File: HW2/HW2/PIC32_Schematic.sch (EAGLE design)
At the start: 22 parts

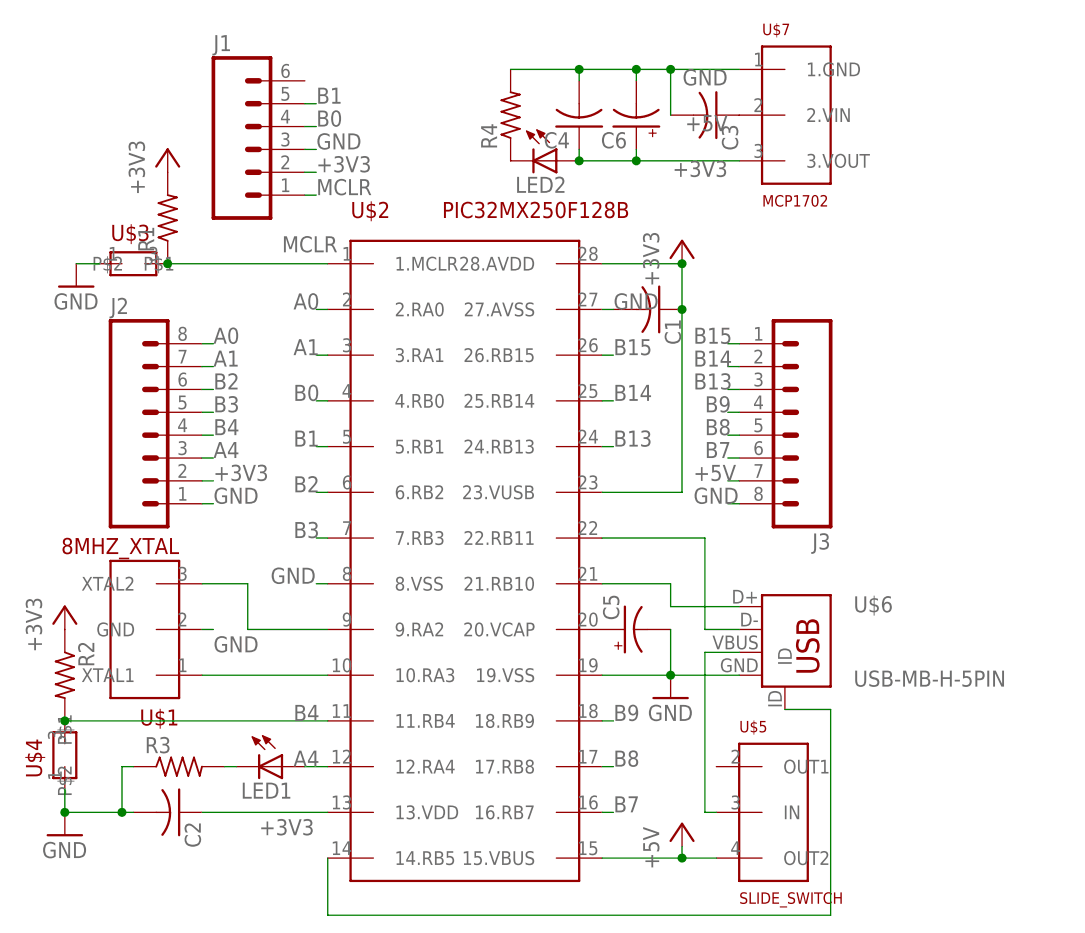
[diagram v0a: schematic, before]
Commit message: Entire schematic is connected (verified).
Formatting and value setting required!
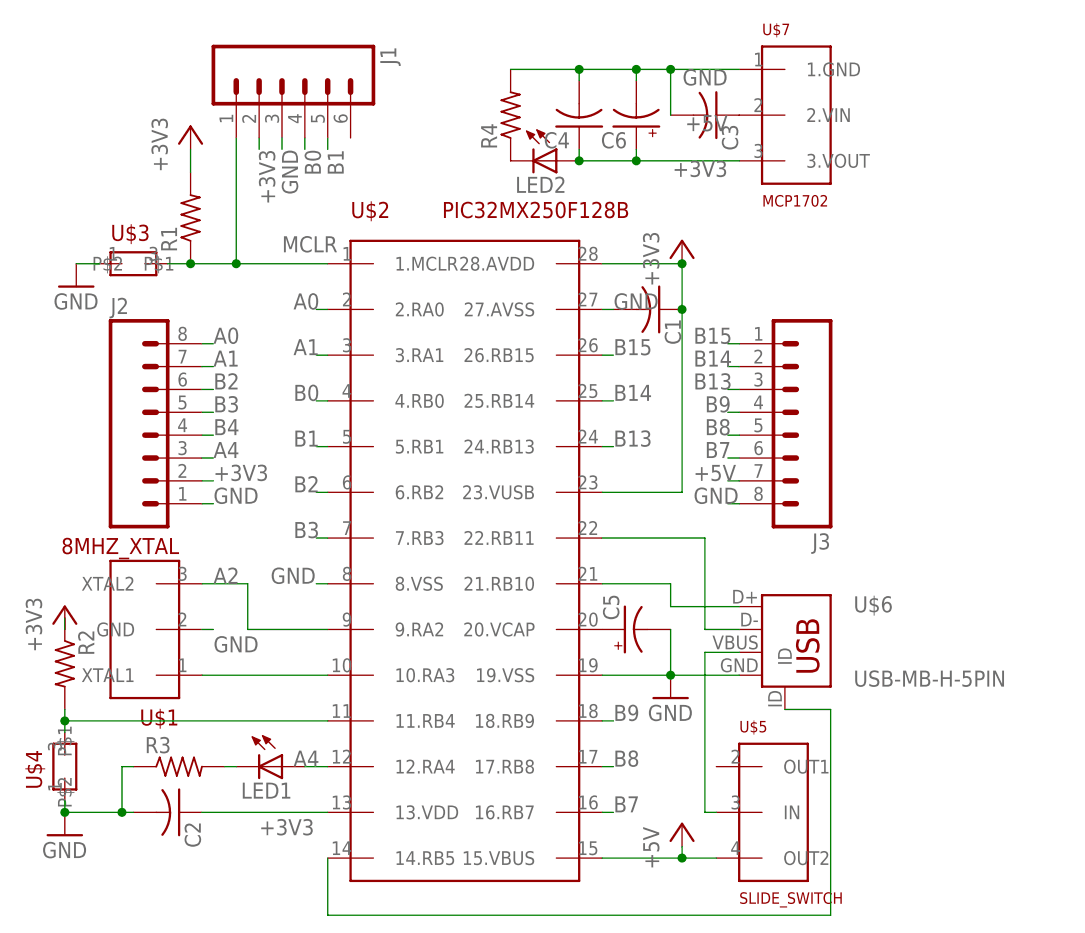
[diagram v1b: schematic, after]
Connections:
- net N$1 renamed GREENLED
- net N$19 renamed A3
- net N$2 renamed VBUS
- new net A2: U$1.XTAL2, U$2.9.RA2
- net GND: no longer U$1.XTAL2, U$2.9.RA2
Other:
- moved on the sheet: J1, R1, R2, U$4
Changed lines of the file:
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@@
 <instance part="U$2" gate="G$1" x="0" y="0"/>
 <instance part="U$3" gate="G$1" x="-36.83" y="33.02"/>
-<instance part="U$4" gate="G$1" x="-44.45" y="-21.59" rot="R90"/>
+<instance part="U$4" gate="G$1" x="-44.45" y="-22.86" rot="R90"/>
 <instance part="U$5" gate="G$1" x="35.56" y="-27.94"/>
 <instance part="U$6" gate="G$1" x="35.56" y="-8.89"/>
 <instance part="U$7" gate="G$1" x="35.56" y="49.53"/>
-<instance part="J1" gate="G$1" x="-22.86" y="45.72"/>
+<instance part="J1" gate="G$1" x="-20.32" y="52.07" rot="R270"/>
 <instance part="J2" gate="G$1" x="-34.29" y="13.97"/>
 <instance part="J3" gate="G$1" x="35.56" y="16.51" rot="R180"/>
 <instance part="LED1" gate="G$1" x="-20.32" y="-22.86" rot="R270"/>
 <instance part="LED2" gate="G$1" x="10.16" y="44.45" rot="R270"/>
-<instance part="R1" gate="G$1" x="-33.02" y="38.1" rot="R90"/>
-<instance part="R2" gate="G$1" x="-44.45" y="-12.7" rot="R270"/>
+<instance part="R1" gate="G$1" x="-30.48" y="38.1" rot="R90"/>
+<instance part="R2" gate="G$1" x="-44.45" y="-11.43" rot="R270"/>
 <instance part="R3" gate="G$1" x="-31.75" y="-22.86"/>
 <instance part="C1" gate="G$1" x="21.59" y="27.94" rot="R270"/>
@@
 <instance part="P+1" gate="1" x="24.13" y="-29.21"/>
 <instance part="GND2" gate="1" x="-43.18" y="30.48"/>
-<instance part="+3V2" gate="G$1" x="-33.02" y="45.72"/>
+<instance part="+3V2" gate="G$1" x="-30.48" y="48.26"/>
 <instance part="GND3" gate="1" x="-44.45" y="-30.48"/>
 <instance part="+3V3" gate="G$1" x="-44.45" y="-5.08"/>
@@
 </segment>
 </net>
-<net name="N$19" class="0">
+<net name="A3" class="0">
 <segment>
 <pinref part="U$2" gate="G$1" pin="10.RA3"/>
@@
 <net name="MCLR" class="0">
 <segment>
-<pinref part="U$2" gate="G$1" pin="1.MCLR"/>
-<wire x1="-15.24" y1="33.02" x2="-33.02" y2="33.02" width="0.1524" layer="91"/>
 <pinref part="U$3" gate="G$1" pin="P$2"/>
 <label x="-20.32" y="34.29" size="1.778" layer="95"/>
-<junction x="-33.02" y="33.02"/>
 <pinref part="R1" gate="G$1" pin="1"/>
-</segment>
-<segment>
+<wire x1="-33.02" y1="33.02" x2="-30.48" y2="33.02" width="0.1524" layer="91"/>
+<pinref part="U$2" gate="G$1" pin="1.MCLR"/>
+<wire x1="-30.48" y1="33.02" x2="-25.4" y2="33.02" width="0.1524" layer="91"/>
+<junction x="-30.48" y="33.02"/>
 <pinref part="J1" gate="G$1" pin="1"/>
-<wire x1="-17.78" y1="40.64" x2="-16.51" y2="40.64" width="0.1524" layer="91"/>
-<label x="-16.51" y="40.64" size="1.778" layer="95"/>
+<wire x1="-25.4" y1="33.02" x2="-15.24" y2="33.02" width="0.1524" layer="91"/>
+<wire x1="-25.4" y1="46.99" x2="-25.4" y2="33.02" width="0.1524" layer="91"/>
+<junction x="-25.4" y="33.02"/>
 </segment>
 </net>
@@
 <pinref part="R1" gate="G$1" pin="2"/>
 <pinref part="+3V2" gate="G$1" pin="+3V3"/>
+<wire x1="-30.48" y1="45.72" x2="-30.48" y2="43.18" width="0.1524" layer="91"/>
 </segment>
 <segment>
 <pinref part="R2" gate="G$1" pin="1"/>
 <pinref part="+3V3" gate="G$1" pin="+3V3"/>
+<wire x1="-44.45" y1="-6.35" x2="-44.45" y2="-7.62" width="0.1524" layer="91"/>
 </segment>
 <segment>
@@
 <segment>
 <pinref part="J1" gate="G$1" pin="2"/>
-<wire x1="-17.78" y1="43.18" x2="-16.51" y2="43.18" width="0.1524" layer="91"/>
-<label x="-16.51" y="43.18" size="1.778" layer="95"/>
+<wire x1="-22.86" y1="46.99" x2="-22.86" y2="45.72" width="0.1524" layer="91"/>
+<label x="-22.86" y="45.72" size="1.778" layer="95" rot="R270"/>
 </segment>
 <segment>
@@
 </segment>
 <segment>
-<pinref part="U$2" gate="G$1" pin="9.RA2"/>
-<pinref part="U$1" gate="G$1" pin="XTAL2"/>
-<wire x1="-29.21" y1="-2.54" x2="-24.13" y2="-2.54" width="0.1524" layer="91"/>
-<wire x1="-24.13" y1="-2.54" x2="-24.13" y2="-7.62" width="0.1524" layer="91"/>
-<wire x1="-24.13" y1="-7.62" x2="-15.24" y2="-7.62" width="0.1524" layer="91"/>
-</segment>
-<segment>
 <pinref part="U$1" gate="G$1" pin="GND"/>
 <wire x1="-29.21" y1="-7.62" x2="-27.94" y2="-7.62" width="0.1524" layer="91"/>
@@
 <segment>
 <pinref part="U$3" gate="G$1" pin="P$1"/>
-<wire x1="-40.64" y1="33.02" x2="-43.18" y2="33.02" width="0.1524" layer="91"/>
 <pinref part="GND2" gate="1" pin="GND"/>
+<wire x1="-43.18" y1="33.02" x2="-40.64" y2="33.02" width="0.1524" layer="91"/>
 </segment>
 <segment>
 <pinref part="U$4" gate="G$1" pin="P$1"/>
 <pinref part="GND3" gate="1" pin="GND"/>
-<wire x1="-44.45" y1="-27.94" x2="-44.45" y2="-25.4" width="0.1524" layer="91"/>
+<wire x1="-44.45" y1="-27.94" x2="-44.45" y2="-26.67" width="0.1524" layer="91"/>
 <pinref part="C2" gate="G$1" pin="2"/>
 <wire x1="-44.45" y1="-27.94" x2="-38.1" y2="-27.94" width="0.1524" layer="91"/>
@@
 <segment>
 <pinref part="J1" gate="G$1" pin="3"/>
-<wire x1="-17.78" y1="45.72" x2="-16.51" y2="45.72" width="0.1524" layer="91"/>
-<label x="-16.51" y="45.72" size="1.778" layer="95"/>
+<wire x1="-20.32" y1="46.99" x2="-20.32" y2="45.72" width="0.1524" layer="91"/>
+<label x="-20.32" y="45.72" size="1.778" layer="95" rot="R270"/>
 </segment>
 <segment>
@@
 </segment>
 <segment>
+<pinref part="R2" gate="G$1" pin="2"/>
 <pinref part="U$4" gate="G$1" pin="P$2"/>
-<pinref part="R2" gate="G$1" pin="2"/>
+<wire x1="-44.45" y1="-16.51" x2="-44.45" y2="-17.78" width="0.1524" layer="91"/>
 <pinref part="U$2" gate="G$1" pin="11.RB4"/>
+<wire x1="-44.45" y1="-17.78" x2="-44.45" y2="-19.05" width="0.1524" layer="91"/>
 <wire x1="-44.45" y1="-17.78" x2="-15.24" y2="-17.78" width="0.1524" layer="91"/>
 <junction x="-44.45" y="-17.78"/>
-<label x="-19.05" y="-17.78" size="1.778" layer="95"/>
 </segment>
 </net>
@@
 <segment>
 <pinref part="J1" gate="G$1" pin="4"/>
-<wire x1="-17.78" y1="48.26" x2="-16.51" y2="48.26" width="0.1524" layer="91"/>
-<label x="-16.51" y="48.26" size="1.778" layer="95"/>
+<wire x1="-17.78" y1="46.99" x2="-17.78" y2="45.72" width="0.1524" layer="91"/>
+<label x="-17.78" y="45.72" size="1.778" layer="95" rot="R270"/>
 </segment>
 <segment>
@@
 <segment>
 <pinref part="J1" gate="G$1" pin="5"/>
-<wire x1="-17.78" y1="50.8" x2="-16.51" y2="50.8" width="0.1524" layer="91"/>
-<label x="-16.51" y="50.8" size="1.778" layer="95"/>
+<wire x1="-15.24" y1="46.99" x2="-15.24" y2="45.72" width="0.1524" layer="91"/>
+<label x="-15.24" y="45.72" size="1.778" layer="95" rot="R270"/>
 </segment>
 <segment>
@@
 </segment>
 </net>
-<net name="N$1" class="0">
+<net name="GREENLED" class="0">
 <segment>
 <pinref part="LED1" gate="G$1" pin="C"/>
@@
 </segment>
 </net>
-<net name="N$2" class="0">
+<net name="VBUS" class="0">
 <segment>
 <pinref part="U$5" gate="G$1" pin="IN"/>
@@
 </segment>
 </net>
+<net name="A2" class="0">
+<segment>
+<pinref part="U$1" gate="G$1" pin="XTAL2"/>
+<label x="-27.94" y="-2.54" size="1.778" layer="95"/>
+<wire x1="-29.21" y1="-2.54" x2="-24.13" y2="-2.54" width="0.1524" layer="91"/>
+<wire x1="-24.13" y1="-2.54" x2="-24.13" y2="-7.62" width="0.1524" layer="91"/>
+<pinref part="U$2" gate="G$1" pin="9.RA2"/>
+<wire x1="-24.13" y1="-7.62" x2="-15.24" y2="-7.62" width="0.1524" layer="91"/>
+</segment>
+</net>

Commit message: Values added; schematic complete
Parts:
- C1, C2, C3, C4: value (none) -> 0.1uF
- C5, C6: value (none) -> 10uF
- LED1: value (none) -> GREEN
- LED2: value (none) -> RED
- R1, R2: value (none) -> 10k
- R3, R4: value (none) -> 330
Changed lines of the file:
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@@
 <part name="J2" library="ME433" deviceset="M08" device=""/>
 <part name="J3" library="ME433" deviceset="M08" device=""/>
-<part name="LED1" library="ME433" deviceset="LED" device="3MM"/>
-<part name="LED2" library="ME433" deviceset="LED" device="3MM"/>
-<part name="R1" library="ME433" deviceset="R-US_" device="0207/10"/>
-<part name="R2" library="ME433" deviceset="R-US_" device="0207/10"/>
-<part name="R3" library="ME433" deviceset="R-US_" device="0207/10"/>
-<part name="C1" library="ME433" deviceset="C-US" device="025-024X044"/>
-<part name="C2" library="ME433" deviceset="C-US" device="025-024X044"/>
-<part name="C3" library="ME433" deviceset="C-US" device="025-024X044"/>
-<part name="C4" library="ME433" deviceset="C-US" device="025-024X044"/>
-<part name="C5" library="ME433" deviceset="CPOL-US" device="E2.5-6"/>
-<part name="C6" library="ME433" deviceset="CPOL-US" device="E2.5-6"/>
+<part name="LED1" library="ME433" deviceset="LED" device="3MM" value="GREEN"/>
+<part name="LED2" library="ME433" deviceset="LED" device="3MM" value="RED"/>
+<part name="R1" library="ME433" deviceset="R-US_" device="0207/10" value="10k"/>
+<part name="R2" library="ME433" deviceset="R-US_" device="0207/10" value="10k"/>
+<part name="R3" library="ME433" deviceset="R-US_" device="0207/10" value="330"/>
+<part name="C1" library="ME433" deviceset="C-US" device="025-024X044" value="0.1uF"/>
+<part name="C2" library="ME433" deviceset="C-US" device="025-024X044" value="0.1uF"/>
+<part name="C3" library="ME433" deviceset="C-US" device="025-024X044" value="0.1uF"/>
+<part name="C4" library="ME433" deviceset="C-US" device="025-024X044" value="0.1uF"/>
+<part name="C5" library="ME433" deviceset="CPOL-US" device="E2.5-6" value="10uF"/>
+<part name="C6" library="ME433" deviceset="CPOL-US" device="E2.5-6" value="10uF"/>
 <part name="+3V1" library="ME433" deviceset="+3V3" device=""/>
 <part name="P+1" library="ME433" deviceset="+5V" device=""/>
@@
 <part name="+3V3" library="ME433" deviceset="+3V3" device=""/>
 <part name="GND1" library="ME433" deviceset="GND" device=""/>
-<part name="R4" library="ME433" deviceset="R-US_" device="0207/10"/>
+<part name="R4" library="ME433" deviceset="R-US_" device="0207/10" value="330"/>
 </parts>
 <sheets>
@@
 <instance part="+3V2" gate="G$1" x="-30.48" y="48.26"/>
 <instance part="GND3" gate="1" x="-44.45" y="-30.48"/>
-<instance part="+3V3" gate="G$1" x="-44.45" y="-5.08"/>
+<instance part="+3V3" gate="G$1" x="-44.45" y="-1.27"/>
 <instance part="GND1" gate="1" x="22.86" y="-15.24"/>
 <instance part="R4" gate="G$1" x="5.08" y="49.53" rot="R90"/>
@@
 <segment>
 <pinref part="U$7" gate="G$1" pin="2.VIN"/>
-<label x="29.21" y="49.53" size="1.778" layer="95" rot="R180"/>
+<label x="35.56" y="49.53" size="1.778" layer="95" rot="R180"/>
 <pinref part="C3" gate="G$1" pin="1"/>
 </segment>
@@
 <pinref part="R2" gate="G$1" pin="1"/>
 <pinref part="+3V3" gate="G$1" pin="+3V3"/>
-<wire x1="-44.45" y1="-6.35" x2="-44.45" y2="-7.62" width="0.1524" layer="91"/>
+<wire x1="-44.45" y1="-6.35" x2="-44.45" y2="-3.81" width="0.1524" layer="91"/>
 </segment>
 <segment>
@@
 <pinref part="U$7" gate="G$1" pin="3.VOUT"/>
 <wire x1="30.48" y1="44.45" x2="19.05" y2="44.45" width="0.1524" layer="91"/>
-<label x="29.21" y="44.45" size="1.778" layer="95" rot="R180"/>
+<label x="31.75" y="43.18" size="1.778" layer="95" rot="R180"/>
 <pinref part="LED2" gate="G$1" pin="A"/>
 <pinref part="C6" gate="G$1" pin="+"/>
@@
 <pinref part="U$2" gate="G$1" pin="26.RB15"/>
 <wire x1="15.24" y1="22.86" x2="16.51" y2="22.86" width="0.1524" layer="91"/>
-<label x="16.51" y="22.86" size="1.778" layer="95"/>
-</segment>
-</net>
+<label x="19.05" y="21.59" size="1.778" layer="95"/>
+</segment>
+</net>
